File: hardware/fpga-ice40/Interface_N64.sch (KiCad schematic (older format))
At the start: 7 parts, among them J6 Conn_02x20_Odd_Even

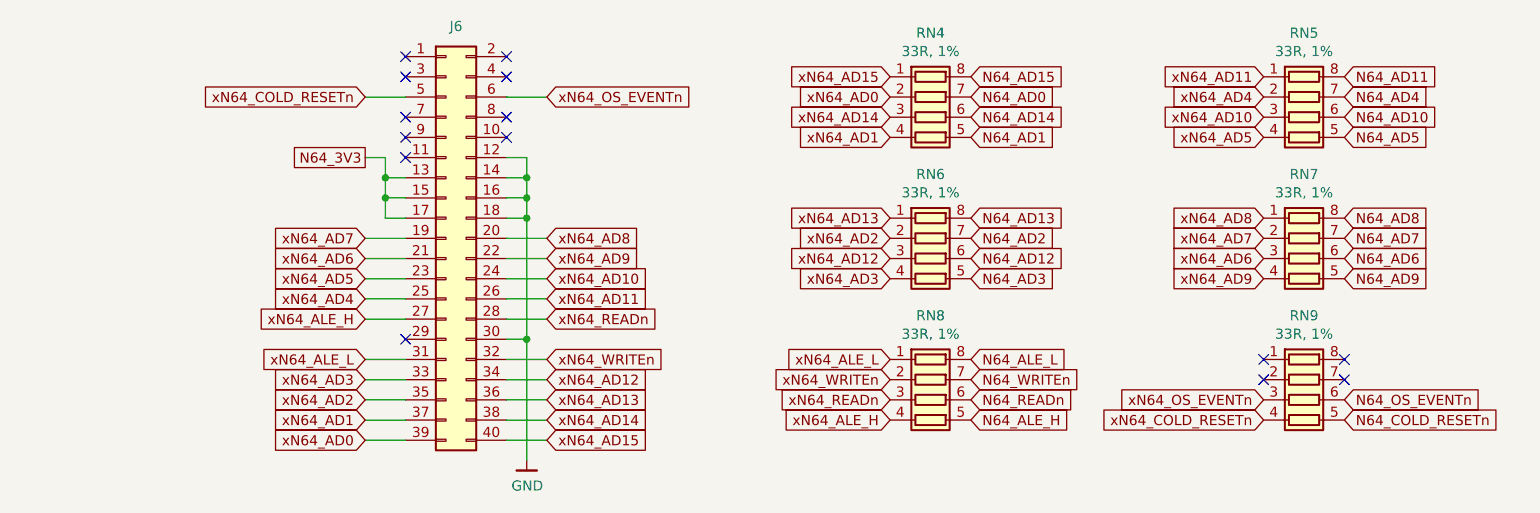
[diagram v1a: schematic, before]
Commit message: Finish layout of power mux
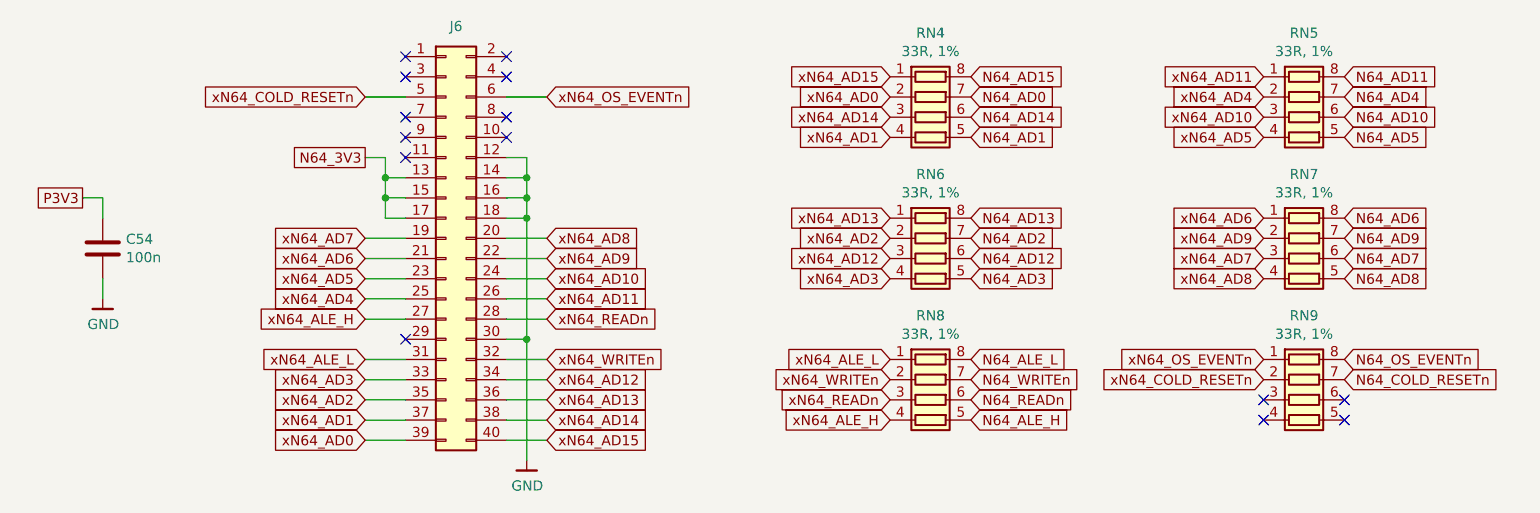
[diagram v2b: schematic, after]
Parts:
- added C54: 100n, Capacitor_SMD:C_0603_1608Metric, symbol Device:C
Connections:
- net GND: now also C54.2
- net N64_AD6: now also RN7.8 (R1.2); no longer RN7.6 (R3.2)
- net N64_AD7: now also RN7.6 (R3.2); no longer RN7.7 (R2.2)
- net N64_AD8: now also RN7.5 (R4.2); no longer RN7.8 (R1.2)
- net N64_AD9: now also RN7.7 (R2.2); no longer RN7.5 (R4.2)
- net N64_COLD_RESETn: now also RN9.7 (R2.2); no longer RN9.5 (R4.2)
- net N64_OS_EVENTn: now also RN9.8 (R1.2); no longer RN9.6 (R3.2)
- net xN64_AD6: now also RN7.1 (R1.1); no longer RN7.3 (R3.1)
- net xN64_AD7: now also RN7.3 (R3.1); no longer RN7.2 (R2.1)
- net xN64_AD8: now also RN7.4 (R4.1); no longer RN7.1 (R1.1)
- net xN64_AD9: now also RN7.2 (R2.1); no longer RN7.4 (R4.1)
- net xN64_COLD_RESETn: now also RN9.2 (R2.1); no longer RN9.4 (R4.1)
- net xN64_OS_EVENTn: now also RN9.1 (R1.1); no longer RN9.3 (R3.1)
- new net P3V3: C54.1
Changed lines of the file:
@@
 Text GLabel 7550 3700 0    50   Input ~ 0
 xN64_AD10
+Text GLabel 7550 4300 0    50   Input ~ 0
+xN64_AD9
 Text GLabel 7550 4500 0    50   Input ~ 0
-xN64_AD9
-Text GLabel 7550 4200 0    50   Input ~ 0
 xN64_AD8
 $Comp
@@
 	0    1    1    0
 $EndComp
-Text GLabel 7550 5200 0    50   Input ~ 0
+Text GLabel 7550 5000 0    50   Input ~ 0
 xN64_COLD_RESETn
-Text GLabel 7550 5100 0    50   Input ~ 0
+Text GLabel 7550 4900 0    50   Input ~ 0
 xN64_OS_EVENTn
 Text GLabel 7550 3600 0    50   Input ~ 0
@@
 Text GLabel 7550 3800 0    50   Input ~ 0
 xN64_AD5
+Text GLabel 7550 4200 0    50   Input ~ 0
+xN64_AD6
 Text GLabel 7550 4400 0    50   Input ~ 0
-xN64_AD6
-Text GLabel 7550 4300 0    50   Input ~ 0
 xN64_AD7
 Text GLabel 6100 3600 2    50   Input ~ 0
@@
 Text GLabel 7950 3700 2    50   Input ~ 0
 N64_AD10
+Text GLabel 7950 4300 2    50   Input ~ 0
+N64_AD9
 Text GLabel 7950 4500 2    50   Input ~ 0
-N64_AD9
-Text GLabel 7950 4200 2    50   Input ~ 0
 N64_AD8
-Text GLabel 7950 5200 2    50   Input ~ 0
+Text GLabel 7950 5000 2    50   Input ~ 0
 N64_COLD_RESETn
-Text GLabel 7950 5100 2    50   Input ~ 0
+Text GLabel 7950 4900 2    50   Input ~ 0
 N64_OS_EVENTn
 Text GLabel 7950 3600 2    50   Input ~ 0
@@
 Text GLabel 7950 3800 2    50   Input ~ 0
 N64_AD5
+Text GLabel 7950 4200 2    50   Input ~ 0
+N64_AD6
 Text GLabel 7950 4400 2    50   Input ~ 0
-N64_AD6
-Text GLabel 7950 4300 2    50   Input ~ 0
 N64_AD7
 Wire Wire Line
 	3200 3900 3200 4000
 Connection ~ 3200 4000
-NoConn ~ 7550 4900
-NoConn ~ 7550 5000
-NoConn ~ 7950 4900
-NoConn ~ 7950 5000
+NoConn ~ 7550 5200
+NoConn ~ 7550 5100
+NoConn ~ 7950 5100
+NoConn ~ 7950 5200
+$Comp
+L Device:C C54
+U 1 1 5F21540A
+P 1800 4350
+F 0 "C54" H 1915 4396 50  0000 L CNN
+F 1 "100n" H 1915 4305 50  0000 L CNN
+F 2 "Capacitor_SMD:C_0603_1608Metric" H 1838 4200 50  0001 C CNN
+F 3 "~" H 1800 4350 50  0001 C CNN
+	1    1800 4350
+	1    0    0    -1
+$EndComp
+Wire Wire Line
+	1800 4500 1800 4600
+Wire Wire Line
+	1800 4200 1800 4100
+Wire Wire Line
+	1800 4100 1700 4100
+Text GLabel 1700 4100 0    50   UnSpc ~ 0
+P3V3
+$Comp
+L ng_power:GND #PWR04
+U 1 1 5F217F51
+P 1800 4600
+F 0 "#PWR04" H 1800 4350 50  0001 C CNN
+F 1 "GND" H 1803 4474 50  0000 C CNN
+F 2 "" H 1700 4250 50  0001 C CNN
+F 3 "" H 1800 4600 50  0001 C CNN
+	1    1800 4600
+	1    0    0    -1
+$EndComp
 $EndSCHEMATC
